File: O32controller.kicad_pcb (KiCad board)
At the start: 4 copper layers, 27 x 27 mm, 56 parts, among them J1 Conn_01x08_MountingPin, J2 BATT+, J3 BATT-, J4 Motor Connection, J5 Motor Connection, J6 Motor Connection, Q1 DMM0022A, Q2 DMM0022A, Q3 DMM0022A, U1 AS5047D, U2 STSPIN32F0A

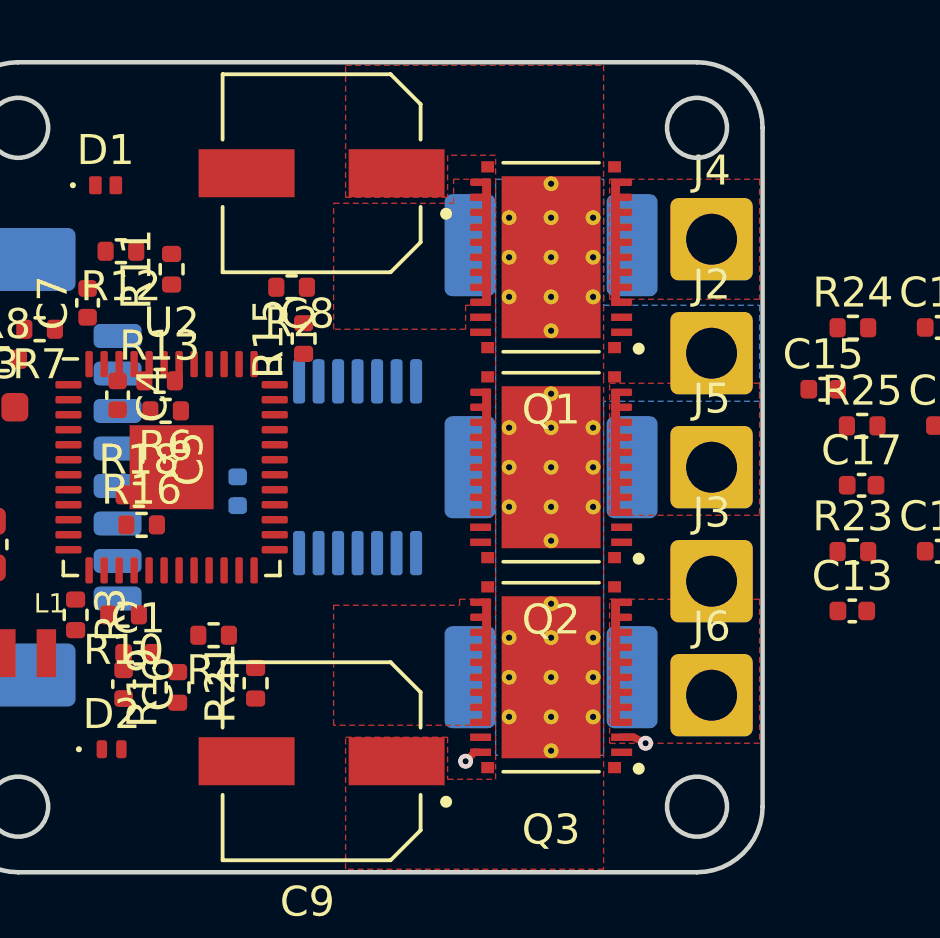
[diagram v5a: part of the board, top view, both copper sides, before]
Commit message: ran into problem routing ground trace
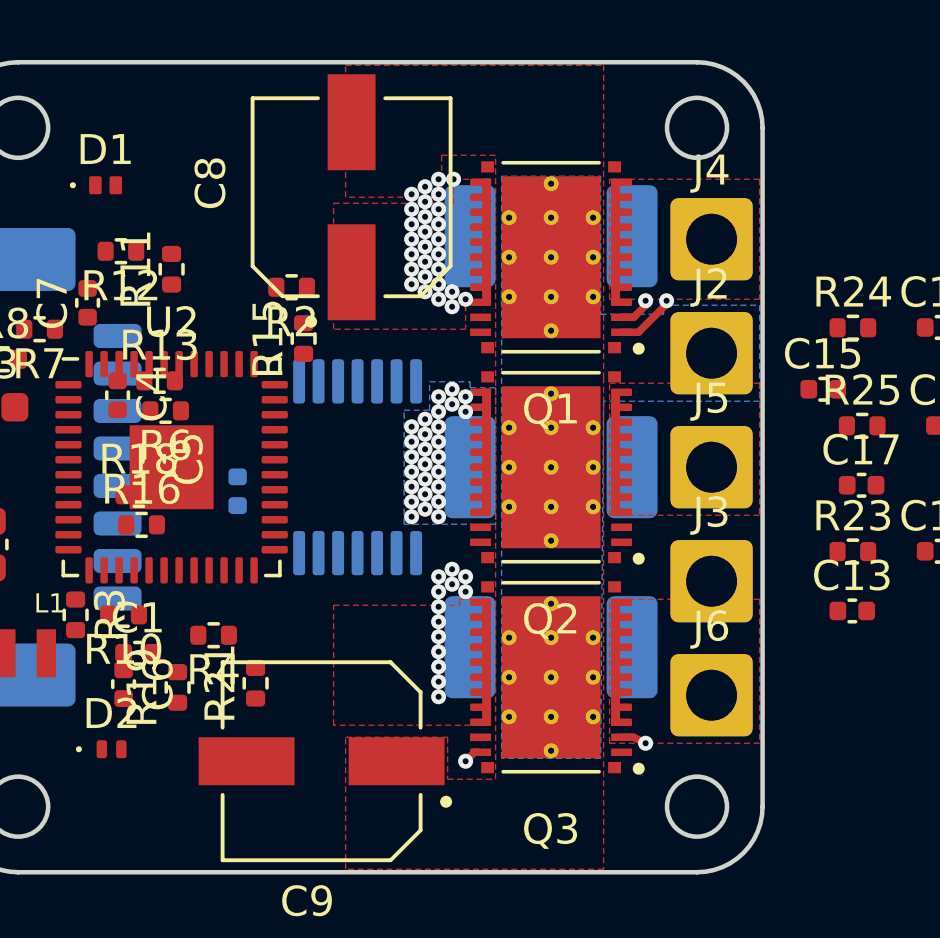
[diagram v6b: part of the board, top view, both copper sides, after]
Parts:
- moved C8 1.28 mm to (49.8, 41.0), turned to 90 degrees
- moved R9 1.00 mm to (56.5, 56.0)
- moved R1 0.30 mm to (56.5, 42.3)
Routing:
- net /OUTU: track 4.31 -> 1.12 mm, vias 0 -> 1
- net /Motor phase U/GH_MOS: track 4.10 -> 2.00 mm, vias 0 -> 1
- net /Motor phase W/Sense_P: vias 0 -> 8
- net /Motor phase V/Sense_P: vias 0 -> 47
- net /Motor phase U/Sense_P: vias 0 -> 13
- added copper zone on B.Cu, net /Motor phase V/Sense_P

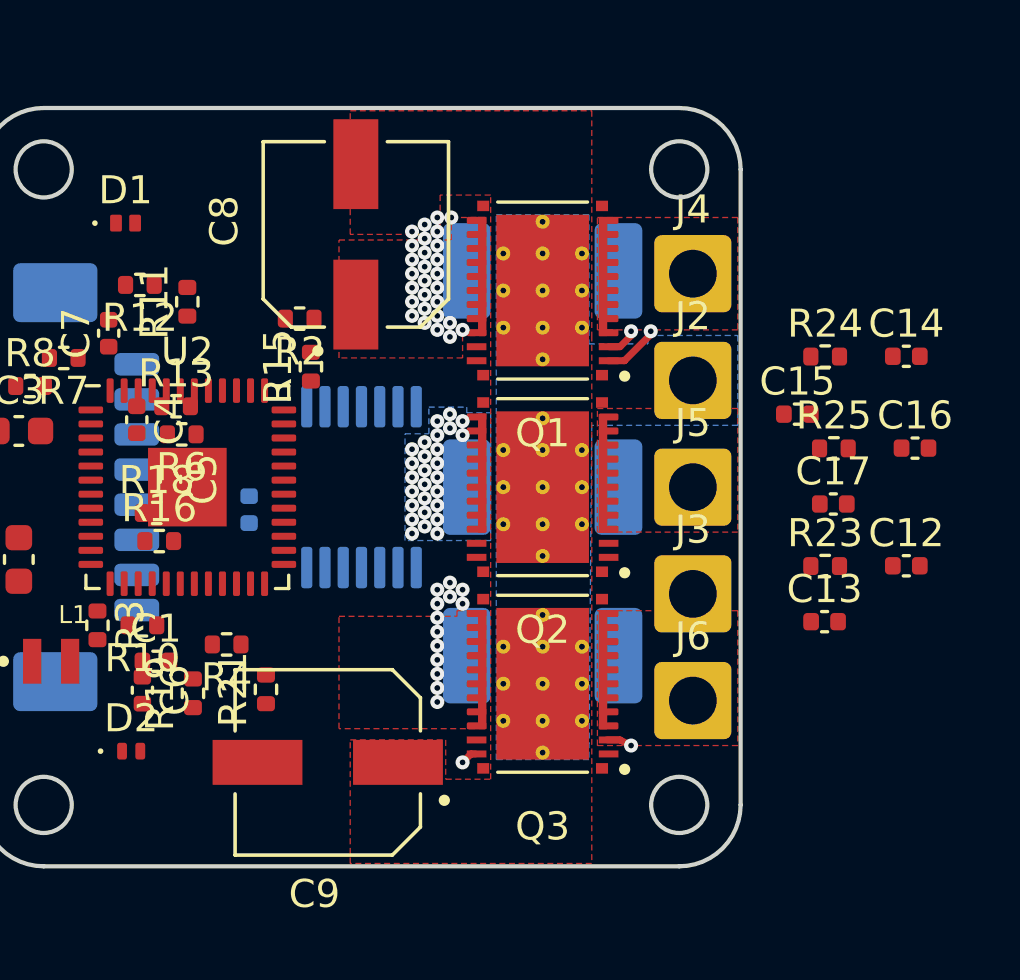
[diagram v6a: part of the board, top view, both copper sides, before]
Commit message: nope I don't think separated motor conns work
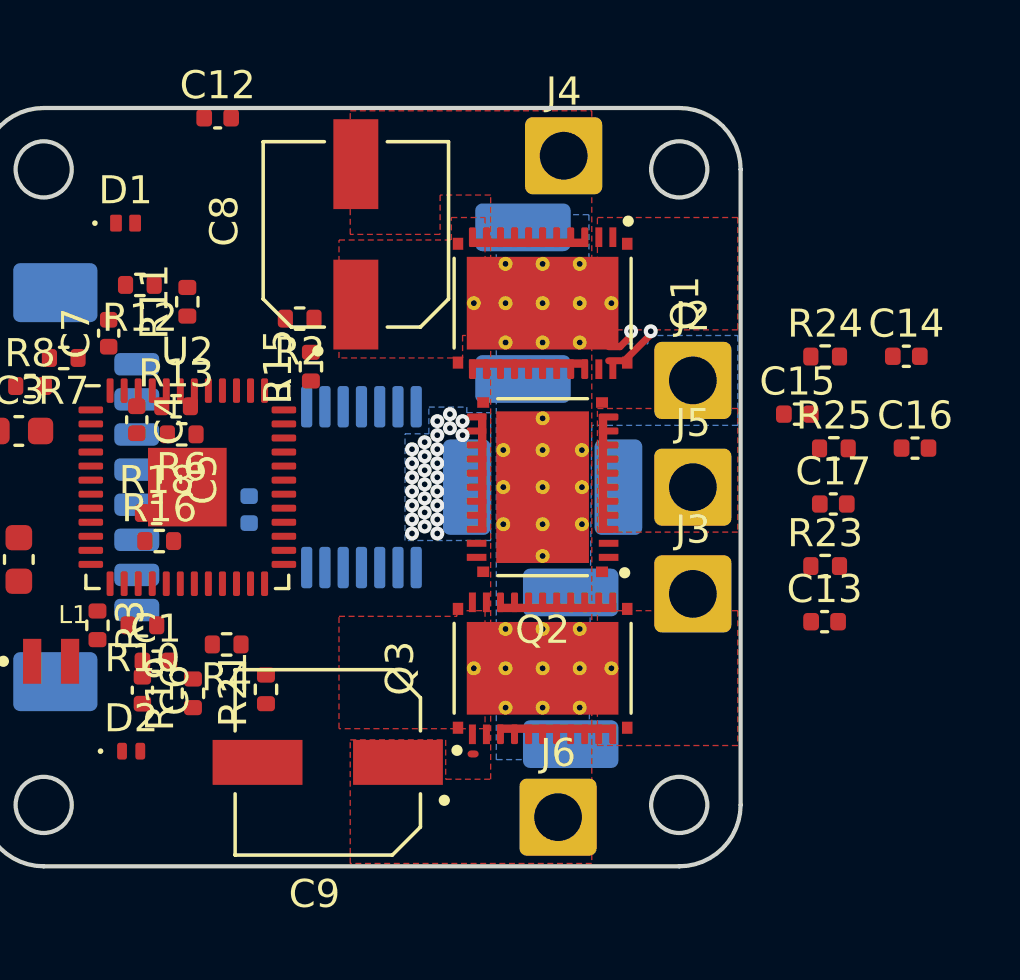
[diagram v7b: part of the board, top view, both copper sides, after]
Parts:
- moved C12 29.3 mm to (44.9, 36.9)
- moved J6 6.35 mm to (57.0, 61.8)
- moved J4 6.23 mm to (57.2, 38.2)
- moved R1 1.35 mm to (55.8, 43.5), turned to -90 degrees
- moved R9 1.10 mm to (57.5, 56.5), turned to 90 degrees
- moved Q3 0.55 mm to (56.5, 56.5), turned to 90 degrees
- moved Q1 0.45 mm to (56.5, 43.5), turned to -90 degrees
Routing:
- net VBUS: track 0.00 -> 1.12 mm
- net /OUTU: track 1.12 -> 0.00 mm
- net /OUTW: track 0.90 -> 0.00 mm, vias 1 -> 0
- net /Motor phase W/GL_MOS: track 0.57 -> 0.00 mm, vias 1 -> 0
- net /Motor phase W/Sense_P: vias 8 -> 0
- net /Motor phase V/Sense_P: vias 47 -> 27
- net /Motor phase U/Sense_P: vias 13 -> 0

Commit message: routed some more
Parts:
- added J7: BATT+, O32controller:SolderWire-Actual_1x01_D1.7mm_OD_2.75mm, F.Cu at (56.5, 61.9)
- added J8: BATT-, O32controller:SolderWire-Actual_1x01_D1.7mm_OD_2.75mm, F.Cu at (61.9, 46.1)
- C12, C13, C14, C15, C16, C17: moved to B.Cu
- Q1, Q2, Q3: value DMM0022A -> CSD88584Q5DCT
- R23, R24, R25: value 2.21R -> 2.2R; moved to B.Cu
- moved C14 16.6 mm to (52.8, 45.6), turned to 180 degrees
- moved C16 15.8 mm to (54.6, 53.2), turned to 180 degrees
- moved R25 11.9 mm to (60.6, 58.9), turned to 180 degrees
- moved C13 11.3 mm to (62.5, 44.2), turned to 180 degrees
- moved R23 10.4 mm to (60.7, 44.2), turned to 180 degrees
- moved J2 9.71 mm to (56.5, 38.1)
- moved C12 9.53 mm to (54.0, 39.6), turned to 180 degrees
- moved C17 9.30 mm to (62.5, 58.9), turned to 180 degrees
- moved R24 8.47 mm to (60.7, 51.5), turned to 180 degrees
- moved R3 7.05 mm to (47.6, 55.0)
- moved J6 6.82 mm to (61.9, 57.0)
- moved J4 6.20 mm to (61.9, 42.3)
- moved C15 5.08 mm to (62.5, 51.5), turned to 180 degrees
- moved R1 1.57 mm to (56.5, 42.0), turned to 180 degrees
- moved R9 1.00 mm to (56.5, 56.5), turned to 180 degrees
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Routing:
- net /Motor phase V/Motor: track 0.00 -> 2.38 mm
- net /Motor phase V/GH_MOS: track 0.00 -> 2.38 mm, vias 0 -> 1
- net /Motor phase U/Motor: track 0.00 -> 2.37 mm
- net /Motor phase W/Motor: track 0.00 -> 2.37 mm
- net /OUTV: track 0.00 -> 2.31 mm, vias 0 -> 1
- net /OUTU: track 0.00 -> 1.81 mm
- net VBUS: track 1.12 -> 0.00 mm, vias 0 -> 3
- net Net-(C17-Pad2): track 0.00 -> 0.86 mm
- net Net-(C13-Pad2): track 0.00 -> 0.86 mm
- net Net-(C15-Pad2): track 0.00 -> 0.84 mm
- net /Motor phase U/GH_MOS: track 2.00 -> 2.72 mm
- net /OUTW: track 0.00 -> 0.60 mm, vias 0 -> 1
- net /Motor phase W/GH_MOS: track 0.15 -> 0.65 mm, vias 0 -> 1
- net unconnected-(U1-Pad14): vias 0 -> 3
- net /Motor phase V/Sense_P: vias 27 -> 20
- added copper zone on B.Cu, net GND
